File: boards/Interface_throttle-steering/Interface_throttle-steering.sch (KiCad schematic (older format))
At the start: 3 parts

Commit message: Fixed wrong footprint.
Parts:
- removed J?: Ampseal_14, symbol Ampseal_14
- added J?: Ultrafit_2, footprints:Ultrafit_2, symbol Ultrafit_2
- added J?: Ampseal_23, symbol Ampseal_23
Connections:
- net labels added: ESTOP_I_out, ESTOP_in
- wire segments 0 -> 12
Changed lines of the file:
@@
 LIBS:contrib
 LIBS:valves
+LIBS:Interface_throttle-steering-cache
 EELAYER 25 0
 EELAYER END
@@
 Comment4 ""
 $EndDescr
-$Comp
-L Ampseal_14 J?
-U 1 1 5A255D30
-P 1300 4900
-F 0 "J?" H 1050 5650 60  0000 C CNN
-F 1 "Ampseal_14" H 1000 4150 60  0000 L CNN
-F 2 "" H 1100 5200 60  0001 C CNN
-F 3 "" H 1100 5200 60  0001 C CNN
-	1    1300 4900
-	1    0    0    -1
-$EndComp
 $Comp
 L micromatch_male_20 J?
@@
 Text Label 1500 5550 0    60   ~ 0
 GND
+Text Label 3500 4250 2    60   ~ 0
+IS_in
+Text Label 3850 4250 0    60   ~ 0
+IS_out
+Wire Wire Line
+	3500 4250 3650 4250
+Wire Wire Line
+	3650 4250 3850 4250
+$Comp
+L Ultrafit_2 J?
+U 1 1 5A260206
+P 1150 6850
+F 0 "J?" H 1150 7000 60  0000 C CNN
+F 1 "Ultrafit_2" H 1250 6650 60  0000 C CNN
+F 2 "footprints:Ultrafit_2" H 1050 6900 60  0001 C CNN
+F 3 "" H 1150 7000 60  0001 C CNN
+F 4 "https://www.digikey.com/product-detail/en/molex-llc/1722861102/WM11570-ND/5344267" H 1250 7100 60  0001 C CNN "PurchasingLink"
+F 5 "Digi-Key" H 1350 7200 60  0001 C CNN "MFN"
+F 6 "WM11570-ND" H 1450 7300 60  0001 C CNN "MPN"
+F 7 "Value" H 1550 7400 60  0001 C CNN "Package"
+	1    1150 6850
+	1    0    0    -1
+$EndComp
+Text Label 1400 6800 0    60   ~ 0
+ESTOP_in
+Text Label 1400 6900 0    60   ~ 0
+ESTOP_I_out
+Text Label 3700 4500 0    60   ~ 0
+Crash_sense
+Wire Wire Line
+	3700 4500 3650 4500
+Wire Wire Line
+	3650 4500 3650 4250
+Connection ~ 3650 4250
+Text Label 3500 4700 2    60   ~ 0
+ESTOP_in
+Text Label 3850 4700 0    60   ~ 0
+BOTS_in
+Wire Wire Line
+	3500 4700 3650 4700
+Wire Wire Line
+	3650 4700 3850 4700
+Text Label 3700 4950 0    60   ~ 0
+BOTS_sense
+Wire Wire Line
+	3700 4950 3650 4950
+Wire Wire Line
+	3650 4950 3650 4700
+Connection ~ 3650 4700
+Text Label 3500 5150 2    60   ~ 0
+ESTOP_I_out
+Text Label 3850 5150 0    60   ~ 0
+ESTOP_out
+Wire Wire Line
+	3500 5150 3650 5150
+Wire Wire Line
+	3650 5150 3850 5150
+Text Label 3700 5400 0    60   ~ 0
+ESTOP_sense
+Wire Wire Line
+	3700 5400 3650 5400
+Wire Wire Line
+	3650 5400 3650 5150
+Connection ~ 3650 5150
+$Comp
+L Ampseal_23 J?
+U 1 1 5A260E79
+P 1300 5350
+F 0 "J?" H 1050 6550 60  0000 C CNN
+F 1 "Ampseal_23" H 1000 4150 60  0000 L CNN
+F 2 "" H 1100 6100 60  0001 C CNN
+F 3 "" H 1100 6100 60  0001 C CNN
+	1    1300 5350
+	1    0    0    -1
+$EndComp
 $EndSCHEMATC

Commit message: Updated Layout
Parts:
- removed J?: Ultrafit_2, footprints:Ultrafit_2, symbol Ultrafit_2
- added J?: Ultrafit_4, footprints:Ultrafit_4, symbol Ultrafit_4
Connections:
- net GND_shield is gone; now on net 5V: J?.12
- net RTD_GND is gone; now on net CAN_low: J?.10
- net 12V: now also J?.11, J?.18; no longer J?.13, J?.9
- net 5V: now also J?.19, J?.3
- net BOTS_in: now also J?.1; no longer J?.2
- net CAN_high: now also J?.16, J?.9; no longer J?.4, J?.8
- net CAN_low: now also J?.17; no longer J?.3, J?.7
- net Crash_sense: no longer J?.1, J?.11
- net ESTOP_I_out: now also J?.2; no longer J?.6
- net GND: now also J?.1, J?.2, J?.21
- net Steering_sense: now also J?.20
- net RTD_LS: now reaches J?.4
- net Crash_Sensor_In/BOTS_Out: now reaches J?.15
- net Crash_Sensor_In/BOTS_Out: now also J?.8
- net BOTS_In/E-Stop_Out: now reaches J?.22
- net E-Stop_In/Connector_to_HVD_Out: now reaches J?.23
- new net BSPD_In/Crash_Sensor_Out: J?.6, J?.7
- new net Throtle_left: J?.4
- new net Throtte_right: J?.13
- no-connect marks 1 -> 0
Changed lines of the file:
@@
 Text Label 1400 3750 0    60   ~ 0
 Crash_sense
-NoConn ~ 1400 3850
 Text Label 1500 4250 0    60   ~ 0
-IS_out
+GND
 Text Label 1500 4350 0    60   ~ 0
-BOTS_in
+GND
 Text Label 1500 4450 0    60   ~ 0
-CAN_low
+5V
 Text Label 1500 4550 0    60   ~ 0
-CAN_high
+Throtle_left
 Text Label 1500 4650 0    60   ~ 0
 GND
 Text Label 1500 4750 0    60   ~ 0
-ESTOP_out
-Text Label 1500 4850 0    60   ~ 0
+BSPD_In/Crash_Sensor_Out
+Text Label 1500 4950 0    60   ~ 0
+Crash_Sensor_In/BOTS_Out
+Text Label 1500 5050 0    60   ~ 0
+CAN_high
+Text Label 1500 5150 0    60   ~ 0
 CAN_low
-Text Label 1500 4950 0    60   ~ 0
-CAN_high
-Text Label 1500 5050 0    60   ~ 0
+Text Label 1500 5250 0    60   ~ 0
 12V
-Text Label 1500 5150 0    60   ~ 0
-RTD_GND
-Text Label 1500 5250 0    60   ~ 0
-IS_in
 Text Label 1500 5350 0    60   ~ 0
-GND_shield
+5V
 Text Label 1500 5450 0    60   ~ 0
-12V
+Throtte_right
 Text Label 1500 5550 0    60   ~ 0
 GND
@@
 Wire Wire Line
 	3650 4250 3850 4250
-$Comp
-L Ultrafit_2 J?
-U 1 1 5A260206
-P 1150 6850
-F 0 "J?" H 1150 7000 60  0000 C CNN
-F 1 "Ultrafit_2" H 1250 6650 60  0000 C CNN
-F 2 "footprints:Ultrafit_2" H 1050 6900 60  0001 C CNN
-F 3 "" H 1150 7000 60  0001 C CNN
-F 4 "https://www.digikey.com/product-detail/en/molex-llc/1722861102/WM11570-ND/5344267" H 1250 7100 60  0001 C CNN "PurchasingLink"
-F 5 "Digi-Key" H 1350 7200 60  0001 C CNN "MFN"
-F 6 "WM11570-ND" H 1450 7300 60  0001 C CNN "MPN"
-F 7 "Value" H 1550 7400 60  0001 C CNN "Package"
-	1    1150 6850
-	1    0    0    -1
-$EndComp
-Text Label 1400 6800 0    60   ~ 0
+Text Label 1500 6800 0    60   ~ 0
 ESTOP_in
-Text Label 1400 6900 0    60   ~ 0
+Text Label 1500 6900 0    60   ~ 0
 ESTOP_I_out
 Text Label 3700 4500 0    60   ~ 0
@@
 	1    0    0    -1
 $EndComp
+Text Label 1500 4850 0    60   ~ 0
+BSPD_In/Crash_Sensor_Out
+Text Label 1500 6050 0    60   ~ 0
+5V
+Text Label 1500 6150 0    60   ~ 0
+Steering_sense
+Text Label 1500 6250 0    60   ~ 0
+GND
+Text Label 1500 6450 0    60   ~ 0
+E-Stop_In/Connector_to_HVD_Out
+Text Label 1500 5650 0    60   ~ 0
+Crash_Sensor_In/BOTS_Out
+Text Label 1500 5750 0    60   ~ 0
+CAN_high
+Text Label 1500 5850 0    60   ~ 0
+CAN_low
+Text Label 1500 5950 0    60   ~ 0
+12V
+Text Label 1500 6350 0    60   ~ 0
+BOTS_In/E-Stop_Out
+Text Label 1400 3850 0    60   ~ 0
+RTD_LS
+$Comp
+L Ultrafit_4 J?
+U 1 1 5A7922D8
+P 1150 7000
+F 0 "J?" H 1150 7300 60  0000 C CNN
+F 1 "Ultrafit_4" H 1150 6800 60  0000 C CNN
+F 2 "footprints:Ultrafit_4" H 1050 7250 60  0001 C CNN
+F 3 "http://www.literature.molex.com/SQLImages/kelmscott/Molex/PDF_Images/987651-1008.pdf" H 1150 7350 60  0001 C CNN
+F 4 "Digi-Key" H 1150 7000 60  0001 C CNN "MFN"
+F 5 "Value" H 1150 7000 60  0001 C CNN "Package"
+F 6 "WM11574-ND" H 1150 7000 60  0001 C CNN "MPN"
+F 7 "WM11564-ND" H 1550 7750 60  0001 C CNN "MPN2"
+F 8 "https://www.digikey.com/products/en?keywords=WM11574-ND" H 1650 7850 60  0001 C CNN "PurchasingLink"
+F 9 "https://www.digikey.com/product-detail/en/molex-llc/1722561004/WM11564-ND/5291228" H 1750 7950 60  0001 C CNN "PurchasingLink2"
+	1    1150 7000
+	1    0    0    -1
+$EndComp

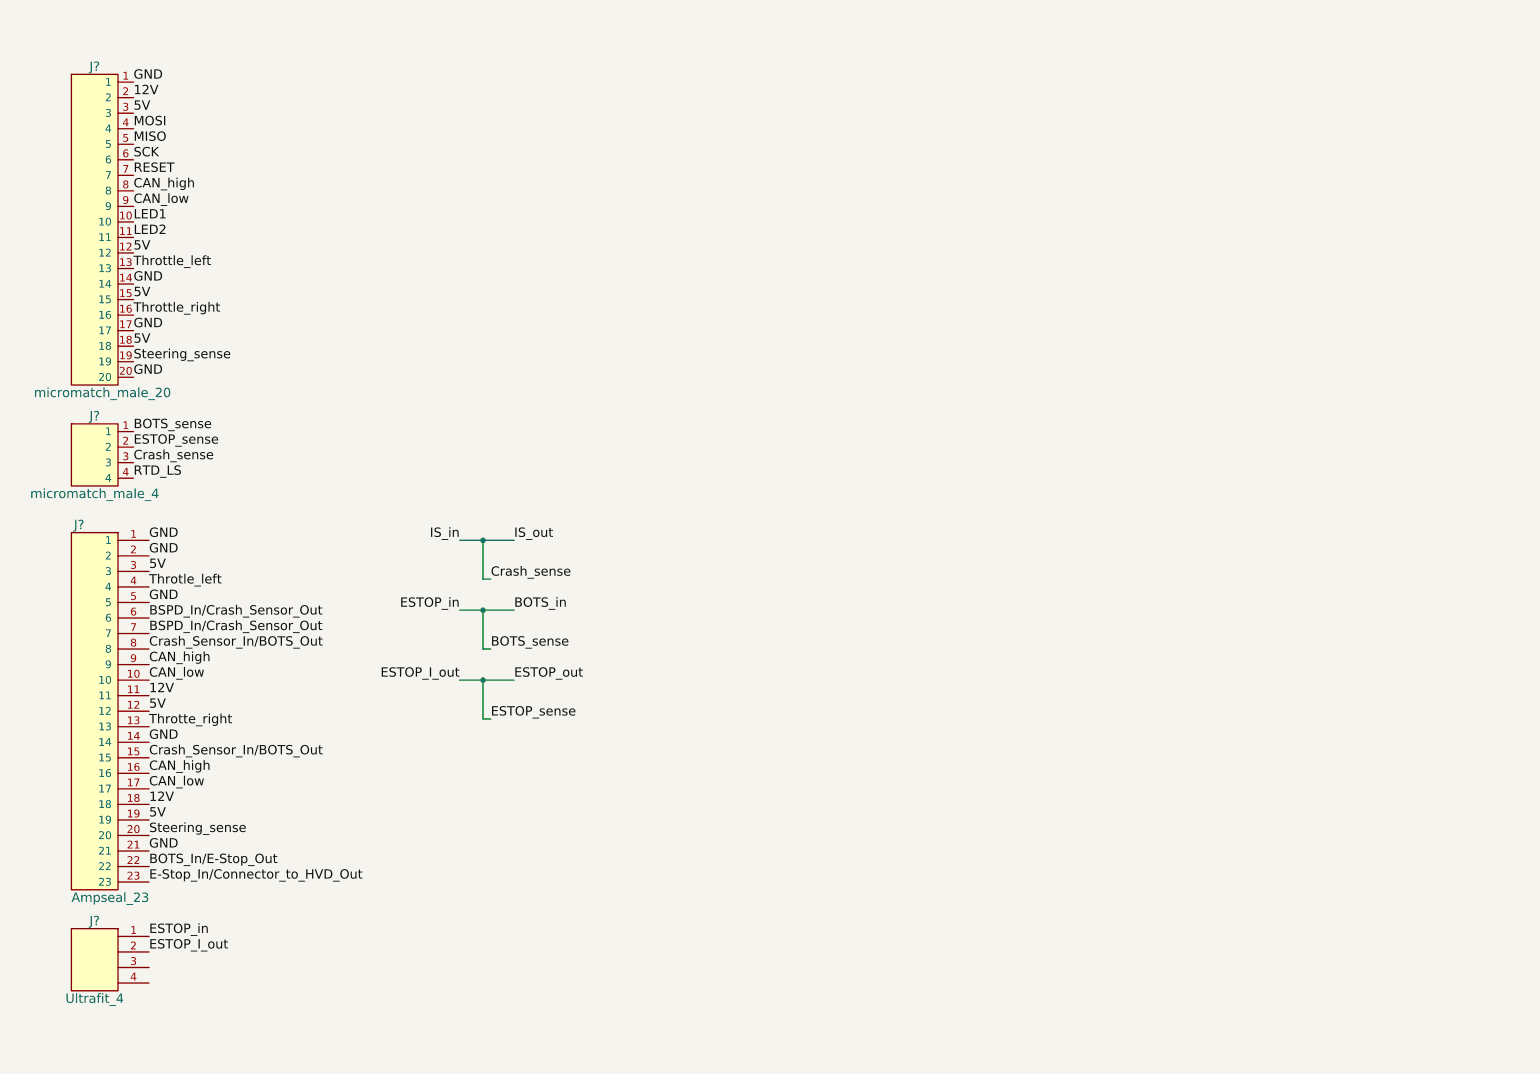
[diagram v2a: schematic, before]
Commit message: Final throttle and interface design pending review
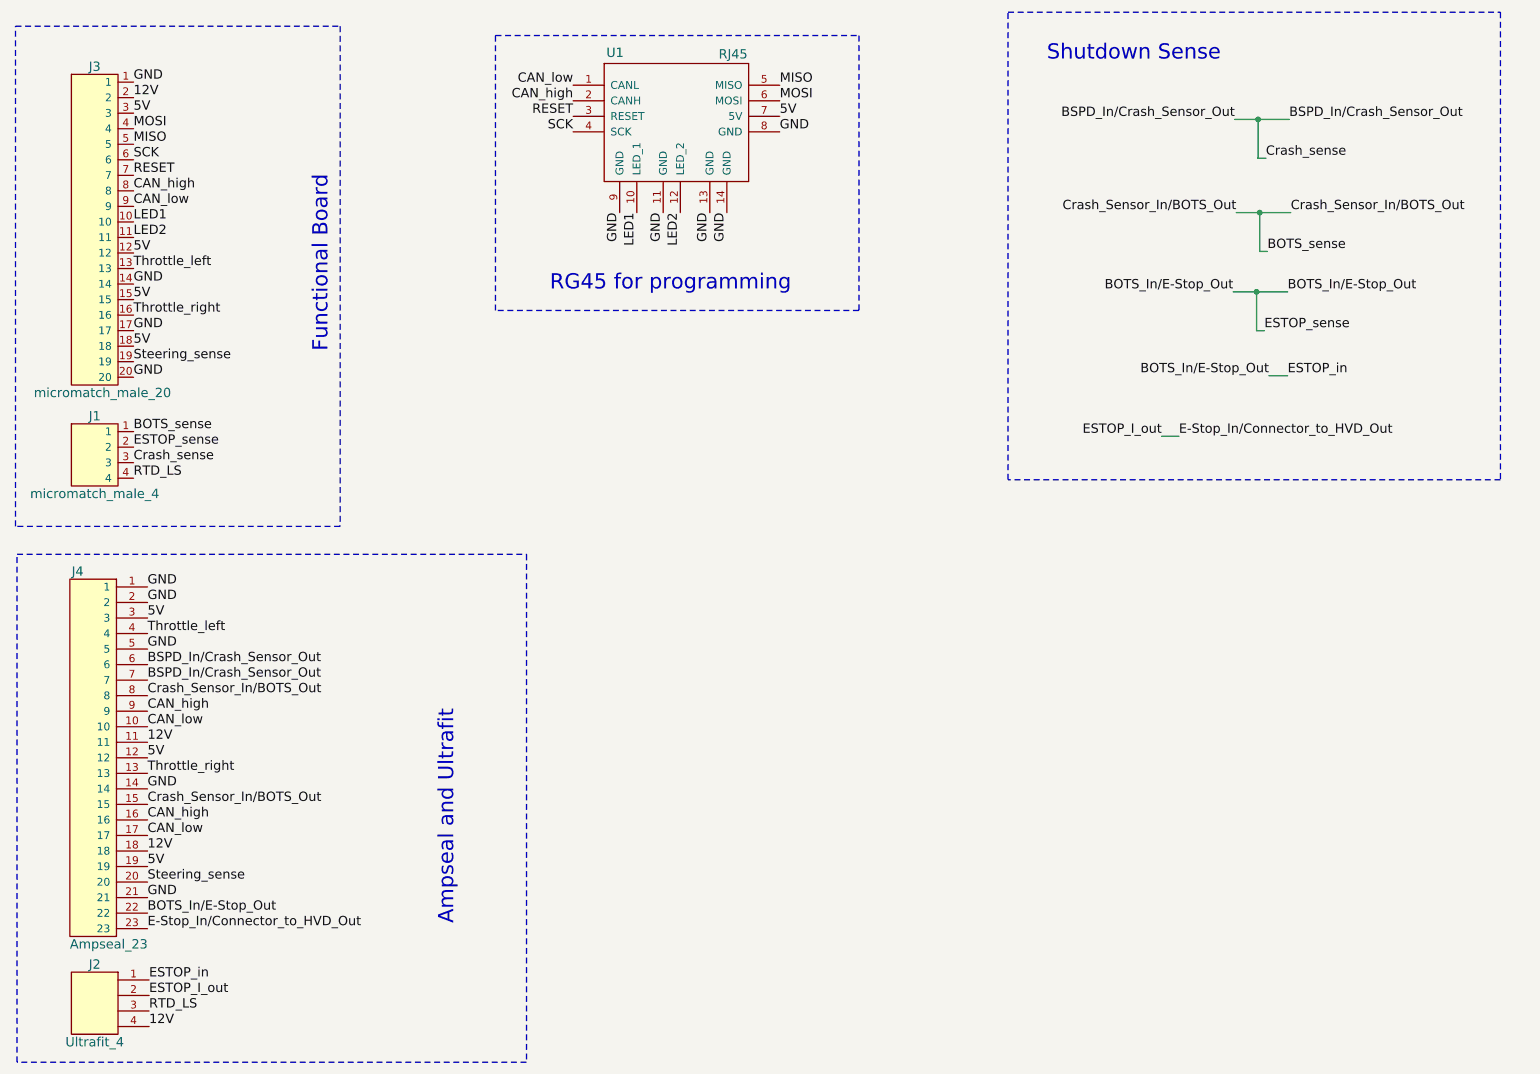
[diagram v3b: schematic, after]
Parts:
- added U1: RJ45, footprints:RJ45-Vertical, symbol RJ45
- J1: renamed from J?; footprint (none) -> footprints:micromatch_female_ra_4
- J3: renamed from J?; footprint (none) -> footprints:micromatch_female_ra_20
- J4: renamed from J?; footprint (none) -> footprints:Ampseal_23
- gave numbers to parts that had none: 1
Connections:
- net Crash_Sensor_In/BOTS_Out is gone; now on net BOTS_sense: J4.15, J4.8
- net Crash_sense is gone; now on net BSPD_In/Crash_Sensor_Out: J1.3
- net Throtle_left is gone; now on net Throttle_left: J4.4
- net Throtte_right is gone; now on net Throttle_right: J4.13
- net 12V: now also J2.4
- net 5V: now also U1.7 (5V)
- net BOTS_In/E-Stop_Out: now also J1.2, J2.1
- net CAN_high: now also U1.2 (CANH)
- net CAN_low: now also U1.1 (CANL)
- net E-Stop_In/Connector_to_HVD_Out: now also J2.2
- net GND: now also U1.11 (GND), U1.13 (GND), U1.14 (GND), U1.8 (GND), U1.9 (GND)
- net LED1: now also U1.10 (LED_1)
- net LED2: now also U1.12 (LED_2)
- net MISO: now also U1.5 (MISO)
- net MOSI: now also U1.6 (MOSI)
- net RESET: now also U1.3 (RESET)
- net RTD_LS: now also J2.3
- net SCK: now also U1.4 (SCK)
- net BOTS_in renamed BOTS_sense
- net BOTS_sense: no longer J2.1
- removed net ESTOP_I_out: J1.2, J2.2
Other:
- note added: "Ampseal and Ultrafit\n"
- note added: "Functional Board"
- note added: "RG45 for programming\n"
- note added: "Shutdown Sense"
- moved on the sheet: J2, J4

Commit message: Rev 2 files for throttle-steering
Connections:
- net BOTS_In/E-Stop_Out: now also J1.1; no longer J1.2
- net BSPD_In/Crash_Sensor_Out: no longer J1.3
- net E-Stop_In/Connector_to_HVD_Out: now also J1.2
- net BOTS_sense renamed Crash_Sensor_In/BOTS_Out
- net Crash_Sensor_In/BOTS_Out: now also J1.3; no longer J1.1
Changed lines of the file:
@@
 Text Label 1490 5850 0    60   ~ 0
 GND
-Wire Wire Line
-	8490 1540 8840 1540
 Text Label 1500 7080 0    60   ~ 0
 ESTOP_in
 Text Label 1500 7180 0    60   ~ 0
 ESTOP_I_out
-Text Label 8690 1790 0    60   ~ 0
+Text Label 8700 1680 0    60   ~ 0
 Crash_sense
 Wire Wire Line
-	8690 1790 8640 1790
-Wire Wire Line
-	8640 1790 8640 1540
-Connection ~ 8640 1540
-Wire Wire Line
-	8500 2140 8850 2140
-Text Label 8700 2390 0    60   ~ 0
+	8500 1430 8850 1430
+Text Label 8680 2190 0    60   ~ 0
 BOTS_sense
 Wire Wire Line
-	8700 2390 8650 2390
+	8700 1680 8650 1680
 Wire Wire Line
-	8650 2390 8650 2140
-Connection ~ 8650 2140
+	8650 1680 8650 1430
+Connection ~ 8650 1430
 Wire Wire Line
-	8480 2650 8830 2650
-Text Label 8680 2900 0    60   ~ 0
+	8480 1940 8830 1940
+Text Label 8430 2870 0    60   ~ 0
 ESTOP_sense
 Wire Wire Line
-	8680 2900 8630 2900
+	8680 2190 8630 2190
 Wire Wire Line
-	8630 2900 8630 2650
-Connection ~ 8630 2650
+	8630 2190 8630 1940
+Connection ~ 8630 1940
 $Comp
 L Ampseal_23 J4
@@
 Text Label 4230 1320 2    60   ~ 0
 CAN_low
-Text Label 8490 1540 2    60   ~ 0
-BSPD_In/Crash_Sensor_Out
-Text Label 8840 1540 0    60   ~ 0
-BSPD_In/Crash_Sensor_Out
-Text Label 8500 2140 2    60   ~ 0
+Text Label 8500 1430 2    60   ~ 0
 Crash_Sensor_In/BOTS_Out
-Text Label 8850 2140 0    60   ~ 0
+Text Label 8850 1430 0    60   ~ 0
 Crash_Sensor_In/BOTS_Out
-Text Label 8480 2650 2    60   ~ 0
+Text Label 8480 1940 2    60   ~ 0
 BOTS_In/E-Stop_Out
-Text Label 8830 2650 0    60   ~ 0
+Text Label 8830 1940 0    60   ~ 0
 BOTS_In/E-Stop_Out
 Text Label 8710 3190 2    60   ~ 0
@@
 Text Label 8830 3190 0    60   ~ 0
 ESTOP_in
-Text Label 8020 3580 2    60   ~ 0
+Text Label 8180 2550 2    60   ~ 0
 ESTOP_I_out
-Text Label 8130 3580 0    60   ~ 0
+Text Label 8570 2550 0    60   ~ 0
 E-Stop_In/Connector_to_HVD_Out
 Wire Wire Line
 	8710 3190 8830 3190
 Wire Wire Line
-	8020 3580 8130 3580
+	8180 2550 8570 2550
 Text Label 1500 7380 0    60   ~ 0
 12V
@@
 	10200 850  10200 3860
 Wire Notes Line
-	10200 3860 7030 3860
+	10200 3440 7030 3440
 Wire Notes Line
 	7030 3860 7030 850
@@
 Text Notes 4080 2650 0    98   ~ 0
 RG45 for programming\n
+Wire Wire Line
+	8430 2870 8330 2870
+Wire Wire Line
+	8330 2870 8330 2550
+Connection ~ 8330 2550
 $EndSCHEMATC

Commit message: Modifed data-logger board
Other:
- note added: "RJ45 for programming\n"
- note removed: "RG45 for programming\n"
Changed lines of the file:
@@
 	3730 2770 3730 1000
 Text Notes 4080 2650 0    98   ~ 0
-RG45 for programming\n
+RJ45 for programming\n
 Wire Wire Line
 	8430 2870 8330 2870
